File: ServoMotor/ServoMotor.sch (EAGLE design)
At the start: 30 parts, among them Q1 TIP120, Q2 TIP120, Y1 16MHz

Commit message: Updated ServoMotor
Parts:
- added 5V_REG1: LP2950CDT-5.0G, LP2950CDT-5.0G:LP2950CDT-5.0G
- added R11, R12: 2.2KΩ, eagle-ltspice:RR1210
- added R7, R8: 3.3KΩ, eagle-ltspice:RR1210
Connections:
- new net N$5: OPTO1.EMITTER, R7.2
- new net N$7: Q2.B, R11.1, R7.1
- new net N$8: 5V_REG1.IN, PWR_SERVO.1
- net N$2: now also R8.2; no longer Q1.B
- net N$3: now also Q1.B, R12.1, R8.1; no longer OPTO1.EMITTER, Q2.B
- net PWR_SERVO_VCC: now also 5V_REG1.OUT; no longer PWR_SERVO.1
- net SERVO_GND: now also 5V_REG1.GND_(NOPAD), 5V_REG1.GND_(TAB)
- net SERVO_VCC: now also R11.2, R12.2
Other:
- moved on the sheet: PWR_SERVO, Q1

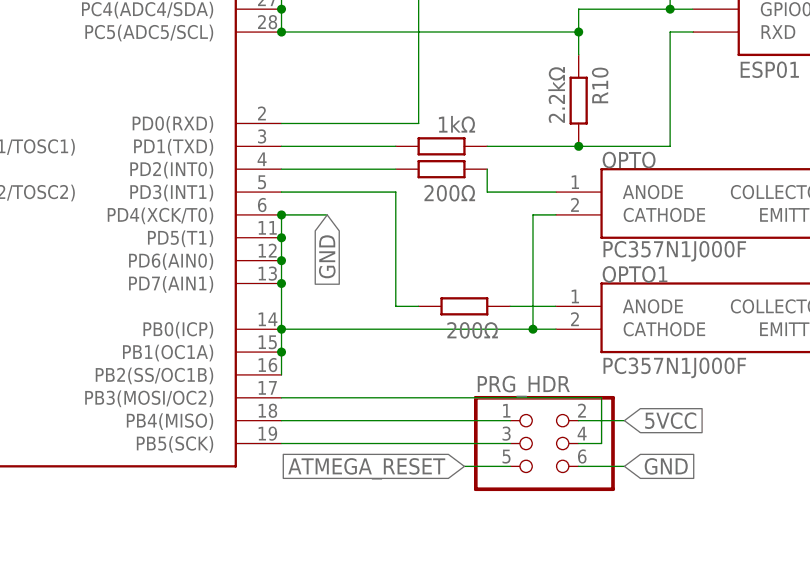
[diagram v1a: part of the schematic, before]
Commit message: Updated Boards, mainly changing up the Servomotor print due to cluttering
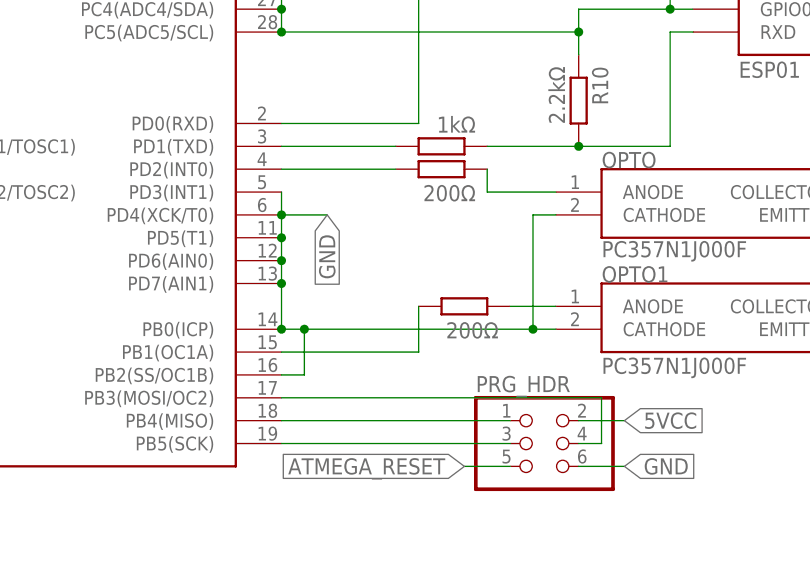
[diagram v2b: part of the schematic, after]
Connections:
- net GND: now also ATMEGA.PD3(INT1); no longer ATMEGA.PB1(OC1A)
- net N$4: now also ATMEGA.PB1(OC1A); no longer ATMEGA.PD3(INT1)
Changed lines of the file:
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@@
 </segment>
 <segment>
-<pinref part="ATMEGA" gate="G$1" pin="PB2(SS/OC1B)"/>
-<pinref part="ATMEGA" gate="G$1" pin="PB1(OC1A)"/>
 <pinref part="ATMEGA" gate="G$1" pin="PD4(XCK/T0)"/>
 <wire x1="30.48" y1="20.32" x2="35.56" y2="20.32" width="0.1524" layer="91"/>
@@
 <pinref part="ATMEGA" gate="G$1" pin="PB0(ICP)"/>
 <junction x="30.48" y="7.62"/>
-<wire x1="30.48" y1="7.62" x2="30.48" y2="5.08" width="0.1524" layer="91"/>
-<junction x="30.48" y="5.08"/>
-<wire x1="30.48" y1="5.08" x2="30.48" y2="2.54" width="0.1524" layer="91"/>
 <label x="35.56" y="20.32" size="1.778" layer="95" rot="R270" xref="yes"/>
 <pinref part="OPTO" gate="G$1" pin="CATHODE"/>
@@
 <pinref part="OPTO1" gate="G$1" pin="CATHODE"/>
 <wire x1="58.42" y1="7.62" x2="60.96" y2="7.62" width="0.1524" layer="91"/>
-<wire x1="58.42" y1="7.62" x2="30.48" y2="7.62" width="0.1524" layer="91"/>
+<wire x1="58.42" y1="7.62" x2="33.02" y2="7.62" width="0.1524" layer="91"/>
 <junction x="58.42" y="7.62"/>
+<pinref part="ATMEGA" gate="G$1" pin="PB2(SS/OC1B)"/>
+<wire x1="33.02" y1="7.62" x2="30.48" y2="7.62" width="0.1524" layer="91"/>
+<wire x1="30.48" y1="2.54" x2="33.02" y2="2.54" width="0.1524" layer="91"/>
+<wire x1="33.02" y1="2.54" x2="33.02" y2="7.62" width="0.1524" layer="91"/>
+<junction x="33.02" y="7.62"/>
+<pinref part="ATMEGA" gate="G$1" pin="PD3(INT1)"/>
+<wire x1="30.48" y1="22.86" x2="30.48" y2="20.32" width="0.1524" layer="91"/>
 </segment>
 </net>
@@
 </segment>
 </net>
-<net name="N$4" class="0">
-<segment>
-<pinref part="R5" gate="G$1" pin="2"/>
-<pinref part="ATMEGA" gate="G$1" pin="PD3(INT1)"/>
-<wire x1="30.48" y1="22.86" x2="43.18" y2="22.86" width="0.1524" layer="91"/>
-<wire x1="43.18" y1="22.86" x2="43.18" y2="10.16" width="0.1524" layer="91"/>
-<wire x1="43.18" y1="10.16" x2="45.72" y2="10.16" width="0.1524" layer="91"/>
-</segment>
-</net>
 <net name="N$2" class="0">
 <segment>
@@
 </segment>
 </net>
+<net name="N$4" class="0">
+<segment>
+<pinref part="ATMEGA" gate="G$1" pin="PB1(OC1A)"/>
+<pinref part="R5" gate="G$1" pin="2"/>
+<wire x1="30.48" y1="5.08" x2="45.72" y2="5.08" width="0.1524" layer="91"/>
+<wire x1="45.72" y1="5.08" x2="45.72" y2="10.16" width="0.1524" layer="91"/>
+</segment>
+</net>

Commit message: wifitracker fix
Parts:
- removed Q2: TIP120, TIP120:TIP120
- removed R7: 3.3KΩ, eagle-ltspice:RR1210
- R11: value 2.2KΩ -> 1KΩ
- R8: value 3.3KΩ -> 500Ω
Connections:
- net N$3 renamed SERVO_VCC_BASE
- net N$4 renamed ATMEG_PWM
- net N$8 renamed BAT_SERVO_VCC
- removed net N$5: OPTO1.EMITTER, R7.2
- removed net N$7: Q2.B, R11.1, R7.1
- net PWR_SERVO_VCC: no longer Q2.C
- net SERVO_GND: now also R11.2, R12.2
- net SERVO_PWM: now also J1.1, OPTO1.EMITTER, R11.1; no longer J1.2, Q2.E
- net SERVO_VCC: now also J1.2; no longer J1.1, R11.2, R12.2
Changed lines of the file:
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@@
 <part name="R5" library="eagle-ltspice" library_urn="urn:adsk.eagle:library:217" deviceset="R" device="R1210" package3d_urn="urn:adsk.eagle:package:13299/1" value="200Ω"/>
 <part name="Q1" library="TIP120" deviceset="TIP120" device=""/>
-<part name="Q2" library="TIP120" deviceset="TIP120" device=""/>
 <part name="PWR_SERVO" library="SparkFun-Connectors" library_urn="urn:adsk.eagle:library:513" deviceset="CONN_02" device="5MM" package3d_urn="urn:adsk.eagle:package:38044/1"/>
 <part name="J1" library="SparkFun-Connectors" library_urn="urn:adsk.eagle:library:513" deviceset="CONN_03" device="" package3d_urn="urn:adsk.eagle:package:38063/1"/>
 <part name="5V_REG1" library="LP2950CDT-5.0G" deviceset="LP2950CDT-5.0G" device=""/>
-<part name="R7" library="eagle-ltspice" library_urn="urn:adsk.eagle:library:217" deviceset="R" device="R1210" package3d_urn="urn:adsk.eagle:package:13299/1" value="3.3KΩ"/>
-<part name="R8" library="eagle-ltspice" library_urn="urn:adsk.eagle:library:217" deviceset="R" device="R1210" package3d_urn="urn:adsk.eagle:package:13299/1" value="3.3KΩ"/>
-<part name="R11" library="eagle-ltspice" library_urn="urn:adsk.eagle:library:217" deviceset="R" device="R1210" package3d_urn="urn:adsk.eagle:package:13299/1" value="2.2KΩ"/>
+<part name="R8" library="eagle-ltspice" library_urn="urn:adsk.eagle:library:217" deviceset="R" device="R1210" package3d_urn="urn:adsk.eagle:package:13299/1" value="500Ω"/>
 <part name="R12" library="eagle-ltspice" library_urn="urn:adsk.eagle:library:217" deviceset="R" device="R1210" package3d_urn="urn:adsk.eagle:package:13299/1" value="2.2KΩ"/>
+<part name="R11" library="eagle-ltspice" library_urn="urn:adsk.eagle:library:217" deviceset="R" device="R1210" package3d_urn="urn:adsk.eagle:package:13299/1" value="1KΩ"/>
 </parts>
 <sheets>
@@
 <attribute name="VALUE" x="125.73" y="19.05" size="1.778" layer="96" align="center-left"/>
 </instance>
-<instance part="Q2" gate="G$1" x="124.46" y="7.62" smashed="yes">
-<attribute name="NAME" x="138.43" y="8.89" size="1.778" layer="95" align="center-left"/>
-<attribute name="VALUE" x="138.43" y="6.35" size="1.778" layer="96" align="center-left"/>
-</instance>
 <instance part="PWR_SERVO" gate="G$1" x="187.96" y="27.94" smashed="yes">
 <attribute name="VALUE" x="185.42" y="23.114" size="1.778" layer="96" font="vector"/>
-<attribute name="NAME" x="185.42" y="36.068" size="1.778" layer="95" font="vector"/>
 </instance>
 <instance part="J1" gate="J$1" x="162.56" y="-7.62" smashed="yes" rot="R180">
@@
 <attribute name="VALUE" x="173.99" y="35.56" size="1.778" layer="96" rot="R180" align="center-left"/>
 </instance>
-<instance part="R7" gate="G$1" x="104.14" y="7.62" smashed="yes" rot="R180">
-<attribute name="NAME" x="107.95" y="6.1214" size="1.778" layer="95" rot="R180"/>
-<attribute name="VALUE" x="108.966" y="11.176" size="1.778" layer="96" rot="R180"/>
-</instance>
 <instance part="R8" gate="G$1" x="104.14" y="20.32" smashed="yes" rot="R180">
 <attribute name="NAME" x="107.95" y="18.8214" size="1.778" layer="95" rot="R180"/>
 <attribute name="VALUE" x="108.966" y="23.876" size="1.778" layer="96" rot="R180"/>
 </instance>
+<instance part="R12" gate="G$1" x="111.76" y="0" smashed="yes" rot="R270">
+<attribute name="NAME" x="113.2586" y="3.81" size="1.778" layer="95" rot="R270"/>
+<attribute name="VALUE" x="108.204" y="4.826" size="1.778" layer="96" rot="R270"/>
+</instance>
 <instance part="R11" gate="G$1" x="119.38" y="0" smashed="yes" rot="R270">
 <attribute name="NAME" x="120.8786" y="3.81" size="1.778" layer="95" rot="R270"/>
 <attribute name="VALUE" x="115.824" y="4.826" size="1.778" layer="96" rot="R270"/>
-</instance>
-<instance part="R12" gate="G$1" x="111.76" y="0" smashed="yes" rot="R270">
-<attribute name="NAME" x="113.2586" y="3.81" size="1.778" layer="95" rot="R270"/>
-<attribute name="VALUE" x="108.204" y="4.826" size="1.778" layer="96" rot="R270"/>
 </instance>
 </instances>
@@
 <segment>
 <pinref part="OPTO1" gate="G$1" pin="COLLECTOR"/>
-<wire x1="99.06" y1="15.24" x2="99.06" y2="10.16" width="0.1524" layer="91"/>
 <pinref part="5V_REG1" gate="G$1" pin="OUT"/>
 <pinref part="Q1" gate="G$1" pin="C"/>
@@
 <wire x1="99.06" y1="27.94" x2="99.06" y2="22.86" width="0.1524" layer="91"/>
 <junction x="121.92" y="27.94"/>
-<pinref part="Q2" gate="G$1" pin="C"/>
-<wire x1="134.62" y1="27.94" x2="134.62" y2="15.24" width="0.1524" layer="91"/>
+<wire x1="134.62" y1="27.94" x2="134.62" y2="10.16" width="0.1524" layer="91"/>
 <junction x="134.62" y="27.94"/>
-<wire x1="99.06" y1="15.24" x2="134.62" y2="15.24" width="0.1524" layer="91"/>
-<junction x="134.62" y="15.24"/>
+<wire x1="99.06" y1="10.16" x2="134.62" y2="10.16" width="0.1524" layer="91"/>
 </segment>
 </net>
@@
 <segment>
 <pinref part="Q1" gate="G$1" pin="E"/>
-<pinref part="J1" gate="J$1" pin="1"/>
 <wire x1="121.92" y1="12.7" x2="121.92" y2="-5.08" width="0.1524" layer="91"/>
-<wire x1="121.92" y1="-5.08" x2="154.94" y2="-5.08" width="0.1524" layer="91"/>
-<pinref part="R11" gate="G$1" pin="2"/>
-<wire x1="119.38" y1="-5.08" x2="121.92" y2="-5.08" width="0.1524" layer="91"/>
-<junction x="121.92" y="-5.08"/>
-<pinref part="R12" gate="G$1" pin="2"/>
-<wire x1="111.76" y1="-5.08" x2="119.38" y2="-5.08" width="0.1524" layer="91"/>
-<junction x="119.38" y="-5.08"/>
-</segment>
-</net>
-<net name="SERVO_PWM" class="0">
-<segment>
-<pinref part="Q2" gate="G$1" pin="E"/>
 <pinref part="J1" gate="J$1" pin="2"/>
-<wire x1="134.62" y1="0" x2="134.62" y2="-7.62" width="0.1524" layer="91"/>
-<wire x1="134.62" y1="-7.62" x2="154.94" y2="-7.62" width="0.1524" layer="91"/>
+<wire x1="121.92" y1="-5.08" x2="121.92" y2="-7.62" width="0.1524" layer="91"/>
+<wire x1="121.92" y1="-7.62" x2="154.94" y2="-7.62" width="0.1524" layer="91"/>
 </segment>
 </net>
 <net name="SERVO_GND" class="1">
 <segment>
-<pinref part="J1" gate="J$1" pin="3"/>
-<wire x1="180.34" y1="-15.24" x2="154.94" y2="-15.24" width="0.1524" layer="91"/>
-<wire x1="154.94" y1="-15.24" x2="154.94" y2="-10.16" width="0.1524" layer="91"/>
 <pinref part="PWR_SERVO" gate="G$1" pin="2"/>
 <wire x1="195.58" y1="30.48" x2="195.58" y2="35.56" width="0.1524" layer="91"/>
@@
 <junction x="195.58" y="30.48"/>
 <wire x1="198.12" y1="20.32" x2="185.42" y2="20.32" width="0.1524" layer="91"/>
-<wire x1="185.42" y1="20.32" x2="185.42" y2="-15.24" width="0.1524" layer="91"/>
-<wire x1="185.42" y1="-15.24" x2="180.34" y2="-15.24" width="0.1524" layer="91"/>
+<wire x1="185.42" y1="20.32" x2="167.64" y2="20.32" width="0.1524" layer="91"/>
+<wire x1="167.64" y1="20.32" x2="167.64" y2="-17.78" width="0.1524" layer="91"/>
+<wire x1="167.64" y1="-17.78" x2="152.4" y2="-17.78" width="0.1524" layer="91"/>
+<wire x1="152.4" y1="-17.78" x2="152.4" y2="-10.16" width="0.1524" layer="91"/>
+<pinref part="J1" gate="J$1" pin="3"/>
+<wire x1="152.4" y1="-10.16" x2="154.94" y2="-10.16" width="0.1524" layer="91"/>
+<pinref part="R12" gate="G$1" pin="2"/>
+<wire x1="152.4" y1="-10.16" x2="119.38" y2="-10.16" width="0.1524" layer="91"/>
+<wire x1="119.38" y1="-10.16" x2="111.76" y2="-10.16" width="0.1524" layer="91"/>
+<wire x1="111.76" y1="-10.16" x2="111.76" y2="-5.08" width="0.1524" layer="91"/>
+<junction x="152.4" y="-10.16"/>
+<pinref part="R11" gate="G$1" pin="2"/>
+<wire x1="119.38" y1="-5.08" x2="119.38" y2="-10.16" width="0.1524" layer="91"/>
+<junction x="119.38" y="-10.16"/>
 </segment>
 </net>
@@
 </segment>
 </net>
-<net name="N$3" class="0">
+<net name="SERVO_VCC_BASE" class="0">
 <segment>
 <pinref part="Q1" gate="G$1" pin="B"/>
@@
 </segment>
 </net>
-<net name="N$5" class="0">
-<segment>
-<pinref part="OPTO1" gate="G$1" pin="EMITTER"/>
-<pinref part="R7" gate="G$1" pin="2"/>
-</segment>
-</net>
-<net name="N$7" class="0">
-<segment>
-<pinref part="R7" gate="G$1" pin="1"/>
-<pinref part="Q2" gate="G$1" pin="B"/>
-<wire x1="109.22" y1="7.62" x2="119.38" y2="7.62" width="0.1524" layer="91"/>
-<pinref part="R11" gate="G$1" pin="1"/>
-<wire x1="119.38" y1="7.62" x2="124.46" y2="7.62" width="0.1524" layer="91"/>
-<wire x1="119.38" y1="7.62" x2="119.38" y2="5.08" width="0.1524" layer="91"/>
-<junction x="119.38" y="7.62"/>
-</segment>
-</net>
-<net name="N$8" class="1">
+<net name="BAT_SERVO_VCC" class="1">
 <segment>
 <pinref part="5V_REG1" gate="G$1" pin="IN"/>
@@
 </segment>
 </net>
-<net name="N$4" class="0">
+<net name="ATMEG_PWM" class="0">
 <segment>
 <pinref part="ATMEGA" gate="G$1" pin="PB1(OC1A)"/>
+<wire x1="30.48" y1="5.08" x2="40.64" y2="5.08" width="0.1524" layer="91"/>
 <pinref part="R5" gate="G$1" pin="2"/>
-<wire x1="30.48" y1="5.08" x2="45.72" y2="5.08" width="0.1524" layer="91"/>
-<wire x1="45.72" y1="5.08" x2="45.72" y2="10.16" width="0.1524" layer="91"/>
-</segment>
-</net>
+<wire x1="40.64" y1="5.08" x2="40.64" y2="10.16" width="0.1524" layer="91"/>
+<wire x1="40.64" y1="10.16" x2="45.72" y2="10.16" width="0.1524" layer="91"/>
+</segment>
+</net>
+<net name="SERVO_PWM" class="0">
+<segment>
+<pinref part="J1" gate="J$1" pin="1"/>
+<wire x1="134.62" y1="0" x2="134.62" y2="-5.08" width="0.1524" layer="91"/>
+<wire x1="134.62" y1="-5.08" x2="154.94" y2="-5.08" width="0.1524" layer="91"/>
+<wire x1="109.22" y1="7.62" x2="119.38" y2="7.62" width="0.1524" layer="91"/>
+<wire x1="119.38" y1="7.62" x2="134.62" y2="7.62" width="0.1524" layer="91"/>
+<wire x1="134.62" y1="7.62" x2="134.62" y2="0" width="0.1524" layer="91"/>
+<pinref part="R11" gate="G$1" pin="1"/>
+<wire x1="119.38" y1="7.62" x2="119.38" y2="5.08" width="0.1524" layer="91"/>
+<junction x="119.38" y="7.62"/>
+<pinref part="OPTO1" gate="G$1" pin="EMITTER"/>
+<wire x1="99.06" y1="7.62" x2="109.22" y2="7.62" width="0.1524" layer="91"/>
+</segment>
+</net>
